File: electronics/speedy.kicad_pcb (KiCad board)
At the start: 2 copper layers, 32 x 32 mm, 131 parts, among them Q1 2N7002, Q2 2N7002, SW1 DFU, SW2 Push, U1 STM32F415RGT6, U10 INA213-SC70, U11 LT1965, U12 MCP73831, U13 DRV8839, U14 DRV8839, U2 NUF2042VX6, U3 MPU-9250, U4 MS5611-01BA, U5 VL53L0X, U6 NRF24L01+, U7 LT1965, U8 LT1965, U9 LTC2955DDB-1, X1 16Mhz 10ppm

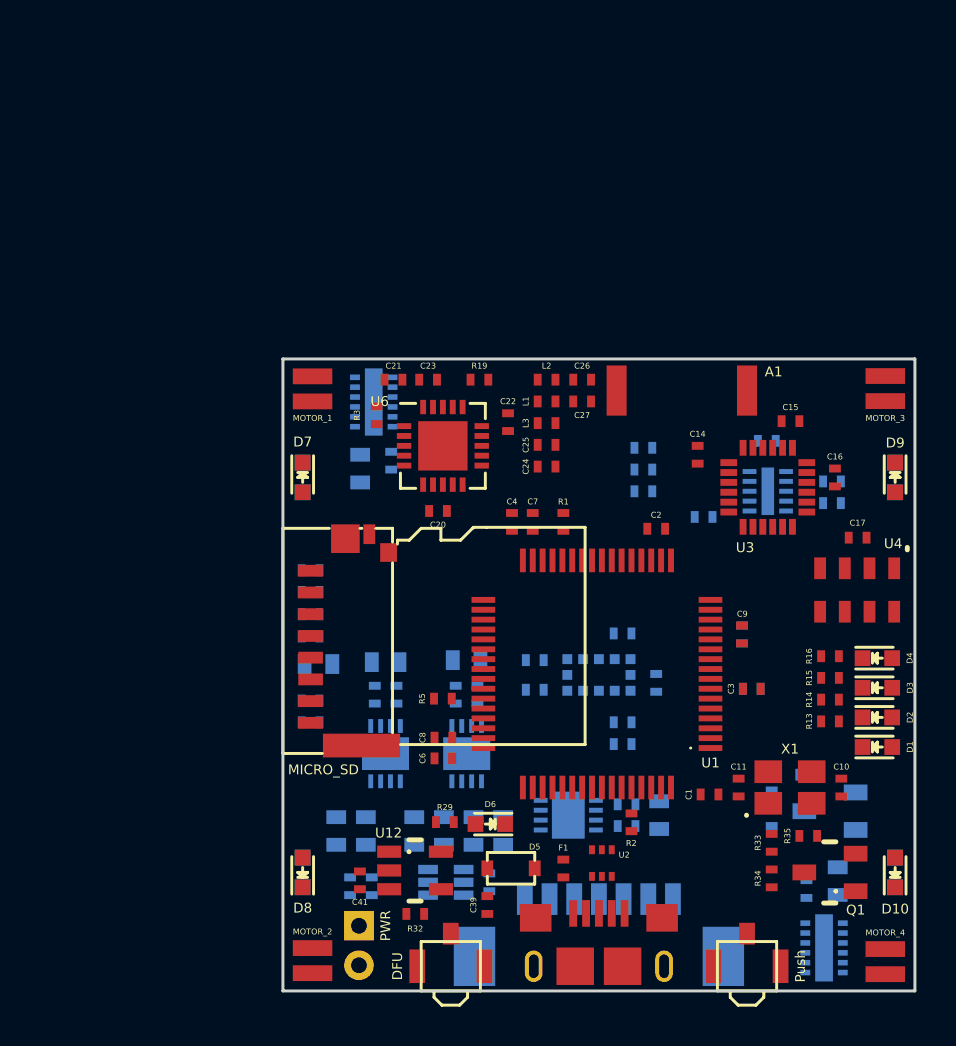
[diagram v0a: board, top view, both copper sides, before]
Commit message: Place components again after schematic update
Increase size of board to 40mmx40mm
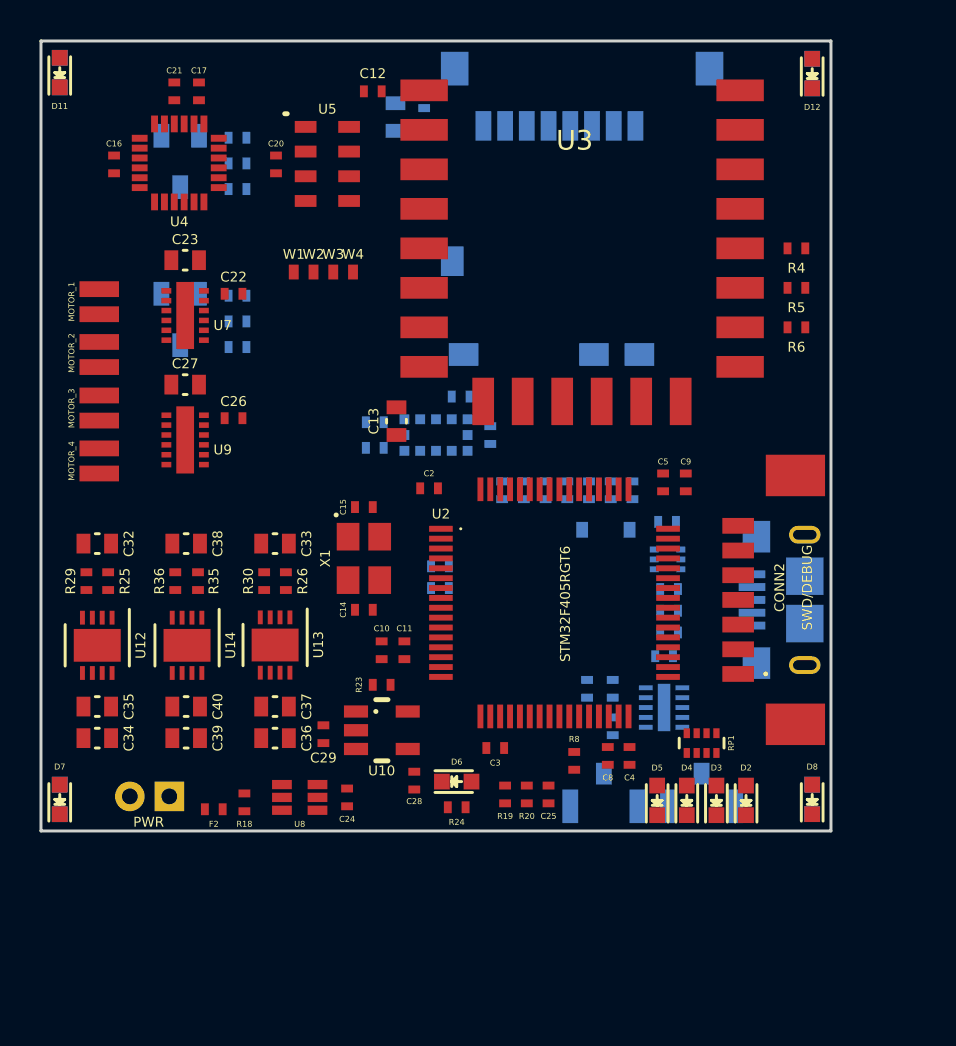
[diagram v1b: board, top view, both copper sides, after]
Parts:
- removed A1: ANTENNA, _div:_ANT-2.45-CHP
- removed C41: 4.7uF, _std:_0402
- removed C42, C45, C46: 10uF, _std:_0603
- removed C43, C44: 0.1uF, _std:_0402
- removed L1: 8.2nH, _std:_0402
- removed L2: 3.9nH, _std:_0402
- removed L3: 2.7nH, _std:_0402
- removed R37: 100, _std:_0402
- removed R38: 40, _std:_0402
- added RP1: 1k, Resistors_SMD:R_Array_Concave_4x0402, F.Cu at (150.8, 110.3)
- added W1: IMU_CS, _div:TestPad, F.Cu at (130.2, 86.5)
- added W2: IMU_SCK, _div:TestPad, F.Cu at (131.2, 86.5)
- added W3: IMU_MISO, _div:TestPad, F.Cu at (132.2, 86.5)
- added W4: IMU_MOSI, _div:TestPad, F.Cu at (133.2, 86.5)
- C1: value 4.7uF -> 0.1uF; moved to B.Cu
- C10: value 10pF -> 1uF
- C11: value 10pF -> 0.1uF
- C12: value 10uF -> 0.1uF; footprint _std:_0603 -> _std:_0402; moved to F.Cu
- C13, C34: value 0.1uF -> 100uF; footprint _std:_0402 -> _std:_0603; moved to F.Cu
- C14: value 0.1uF -> 10pF
- C15: value 10nF -> 10pF
- C17: value 0.1uF -> 10nF
- C2: value 0.1uF -> 4.7uF
- C21: value 33nF -> 0.1uF
- C22: value 10nF -> 0.1uF
- C23: value 1nF -> 10uF; footprint _std:_0402 -> _std:_0603
- C24: value 2.2nF -> 0.1uF
- C25: value 4.7pF -> 0.1uF
- C26: value 1.5pF -> 0.1uF
- C27: value 1pF -> 10uF; footprint _std:_0402 -> _std:_0603
- C28, C29: value 100uF -> 4.7uF; footprint _std:_0603 -> _std:_0402; moved to F.Cu
- C31: value 10uF -> 0.1uF; footprint _std:_0603 -> _std:_0402
- C32, C35, C38, D11, D12, F2, R6: moved to F.Cu
- C33, C40: value 0.1uF -> 10uF; footprint _std:_0402 -> _std:_0603; moved to F.Cu
- C36: value 10uF -> 100uF; moved to F.Cu
- C37: value 100uF -> 10uF; moved to F.Cu
- C39: value 4.7uF -> 100uF; footprint _std:_0402 -> _std:_0603
- C5: value 1uF -> 0.1uF; moved to F.Cu
- C6: value 0.1uF -> 10uF; footprint _std:_0402 -> _std:_0603; moved to B.Cu
- C7: value 2.2uF -> 0.1uF; moved to B.Cu
- C9: value 0.1uF -> 2.2uF
- CONN1: value SWD/DEBUG -> MICRO_USB; footprint _connectors:_Molex-PicoBlade-SMD-7 -> _connectors:_Micro-USB-AB-receptacle-SMT-th
- CONN2: value MICRO_SD -> SWD/DEBUG; footprint _div:_Molex-microSD-WM6701 -> _connectors:_Molex-PicoBlade-SMD-7
- CONN3: value MICRO_USB -> MICRO_SD; footprint _connectors:_Micro-USB-AB-receptacle-SMT-th -> _div:_Molex-microSD-502570-0893; moved to B.Cu
- CONN4: value PWR -> MOTOR_1; footprint _connectors:_Pin2mm_2 -> _connectors:_Solder_Pad1.27_2
- CONN5: value MOTOR_1 -> PWR; footprint _connectors:_Solder_Pad1.27_2 -> _connectors:_Pin2mm_2
- D1: value POWER -> SBR130S3-7; footprint _std:_LED_0603 -> _std:_SOD-323; moved to B.Cu
- D10, D9, Q1, SW1: moved to B.Cu
- D2: value ERROR -> POWER
- D3: value STATUS -> ERROR
- D4: value HEARTBEAT -> STATUS
- D5: value SBR130S3-7 -> DEBUG; footprint _std:_SOD-323 -> _std:_LED_0603
- D6: value CHARGE_LED -> CHARGE
- F1: value 500mA -> 0ZCJ0050AF2E; moved to B.Cu
- R1: value 47k -> 100k; moved to B.Cu
- R13, R16: value 1k -> 10k; moved to B.Cu
- R14, R15: value 1k -> 47k; moved to B.Cu
- R18: value 10k -> 10m; moved to F.Cu
- R19: value 22k -> 2.8k
- R2, R3: value 47k -> 4.7k; moved to B.Cu
- R20: value 10m -> 2k; moved to F.Cu
- R22: value 3.3k -> 10k
- R23: value 2.05k -> 2k; moved to F.Cu
- R24: value 3.3k -> 330; moved to F.Cu
- R25: value 2.05k -> 3.3k; moved to F.Cu
- R26: value 10k -> 3.3k; moved to F.Cu
- R27: value 2.8k -> 100
- R28: value 2k -> 100
- R29: value 330 -> 2.05k
- R30: value 3.3k -> 2.05k; moved to F.Cu
- R31: value 2.05k -> 10k
- R32: value 2k -> 10k; moved to B.Cu
- R33: value 10k -> 40; moved to B.Cu
- R34: value 100 -> 40; moved to B.Cu
- R35: value 40 -> 3.3k
- R36: value 10k -> 2.05k; moved to F.Cu
- R4: value 100k -> 10k; moved to F.Cu
- R5: value 47k -> 10k
- R7: value 4.7k -> 47k
- R8: value 10k -> 47k; moved to F.Cu
- R9: value 4.7k -> 10k
- SW2: value Push -> PushButton; moved to B.Cu
- U1: value STM32F415RGT6 -> NUF2042VX6; footprint _lqfp:_LQFP64 -> _std:SOT-563_6-lead; moved to B.Cu
- U10: value INA213-SC70 -> MCP73831; footprint _std:SC70 -> _std:_TSOT23-5; moved to F.Cu
- U11: value LT1965 -> LTC2955DDB-1; footprint Housings_DFN_QFN:DFN-8-1EP_3x3mm_Pitch0.5mm -> Housings_DFN_QFN:DFN-10-1EP_2x3mm_Pitch0.5mm
- U12: value MCP73831 -> LT1965; footprint _std:_TSOT23-5 -> Housings_DFN_QFN:DFN-8-1EP_3x3mm_Pitch0.5mm
- U13, U14: value DRV8839 -> LT1965; footprint _div:TI-DRV8839_PWSON-N12 -> Housings_DFN_QFN:DFN-8-1EP_3x3mm_Pitch0.5mm; moved to F.Cu
- U2: value NUF2042VX6 -> STM32F405RGT6; footprint _std:SOT-563_6-lead -> _lqfp:_LQFP64
- U3: value MPU-9250 -> ESP-12E; footprint _sensors:_MPU-9XX0 -> _esp:ESP-12-E
- U4: value MS5611-01BA -> MPU-9250; footprint _sensors:_MS5611-01BA -> _sensors:_MPU-9XX0
- U5: value VL53L0X -> MS5611-01BA; footprint _sensors:ST-VL53L0X -> _sensors:_MS5611-01BA; moved to F.Cu
- U6: value NRF24L01+ -> VL53L0X; footprint Housings_DFN_QFN:QFN-20-1EP_4x4mm_Pitch0.5mm -> _sensors:ST-VL53L0X; moved to B.Cu
- U7: value LT1965 -> DRV8839; footprint Housings_DFN_QFN:DFN-8-1EP_3x3mm_Pitch0.5mm -> _div:TI-DRV8839_PWSON-N12; moved to F.Cu
- U8: value LT1965 -> INA213-SC70; footprint Housings_DFN_QFN:DFN-8-1EP_3x3mm_Pitch0.5mm -> _std:SC70; moved to F.Cu
- U9: value LTC2955DDB-1 -> DRV8839; footprint Housings_DFN_QFN:DFN-10-1EP_2x3mm_Pitch0.5mm -> _div:TI-DRV8839_PWSON-N12; moved to F.Cu
- moved Q1 51.9 mm to (123.5, 79.5), turned to 0 degrees
- moved D12 48.0 mm to (156.4, 76.4)
- moved CONN8 47.2 mm to (120.3, 96.0)
- moved D13 47.0 mm to (118.3, 76.3), turned to 90 degrees
- moved D9 45.3 mm to (118.3, 113.2), turned to 90 degrees
- moved R33 44.8 mm to (127.3, 79.7), turned to 0 degrees
- moved Q2 43.3 mm to (123.5, 87.5), turned to 0 degrees
- moved CONN3 42.6 mm to (147.5, 79.0), turned to 180 degrees
- moved D14 40.7 mm to (156.4, 76.4)
- moved U4 40.6 mm to (124.4, 80.9), turned to 180 degrees
- moved C17 40.3 mm to (125.4, 77.3), turned to 90 degrees
- moved R34 40.0 mm to (127.3, 87.7), turned to 0 degrees
- moved CONN7 39.8 mm to (120.3, 93.3), turned to 270 degrees
- moved C16 39.8 mm to (121.1, 81.0), turned to 270 degrees
- moved U14 35.7 mm to (124.8, 105.3)
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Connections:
- C1 pad 1: VCC -> /STM32F4_NRST
- C10 pad 1: Net-(C10-Pad1) -> VCCA
- C11 pad 1: Net-(C11-Pad1) -> VCCA
- C12 pad 1: SD_VCC -> /WIFI_RST_N
- C13 pad 1: SD_VCC -> VCC
- C14 pad 1: VCCA -> Net-(C14-Pad1)
- C15 pad 1: VCCA -> Net-(C15-Pad1)
- C16 pad 1: Net-(C16-Pad1) -> VCCA
- C20 pad 1: VCC -> VCCA
- C21 pad 1: GND -> Net-(C21-Pad1)
- C21 pad 2: Net-(C21-Pad2) -> GND
- C23 pad 1: VCC -> +BATT
- C24 pad 1: Net-(C24-Pad1) -> VCC
- C25 pad 1: Net-(C24-Pad1) -> /VOLTAGE_BAT_SENSE
- C26 pad 1: Net-(C26-Pad1) -> VCC
- C26 pad 2: Net-(A1-Pad1) -> GND
- C27 pad 1: Net-(A1-Pad1) -> +BATT
- C28 pad 1: +BATT -> +5V_protected
- C3 pad 1: /STM32F4_NRST -> VCC
- C31 pad 1: +BATT -> Net-(C31-Pad1)
- C32 pad 1: +BATT -> VCC
- C33 pad 1: Net-(C33-Pad1) -> SD_VCC
- C34 pad 1: VCC -> +BATT
- C35 pad 1: VCC -> +BATT
- C36 pad 1: VCCA -> +BATT
- C38 pad 1: +BATT -> VCCA
- C39 pad 1: /V_USB -> +BATT
- C40 pad 1: /VOLTAGE_BAT_SENSE -> +BATT
- C5 pad 1: VCCA -> VCC
- C6 pad 1: VCC -> SD_VCC
- C7 pad 1: Net-(C7-Pad1) -> SD_VCC
- C9 pad 1: VCCA -> Net-(C9-Pad1)
- CONN1 pad 1: VCC -> Net-(CONN1-Pad1)
- CONN1 pad 2: GND -> Net-(CONN1-Pad2)
- CONN1 pad 3: /STM32F4_NRST -> Net-(CONN1-Pad3)
- CONN1 pad 4: /STM32F4_SWDIO -> Net-(CONN1-Pad4)
- CONN1 pad 5: /STM32F4_SWCLK -> GND
- CONN1 pad 6: /UART3_TX -> Net-(CONN1-Pad6)
- CONN2 pad 1: /SDIO_D2 -> VCC
- CONN2 pad 2: /SDIO_D3 -> GND
- CONN2 pad 3: /SDIO_CMD -> /STM32F4_NRST
- CONN2 pad 4: SD_VCC -> /STM32F4_SWDIO
- CONN2 pad 5: /SDIO_CLK -> /STM32F4_SWCLK
- CONN2 pad 6: GND -> /UART3_TX
- CONN2 pad 7: /SDIO_D0 -> /UART3_RX
- CONN3 pad 1: Net-(CONN3-Pad1) -> /SDIO_D2
- CONN3 pad 2: Net-(CONN3-Pad2) -> /SDIO_D3
- CONN3 pad 3: Net-(CONN3-Pad3) -> /SDIO_CMD
- CONN3 pad 4: Net-(CONN3-Pad4) -> SD_VCC
- CONN3 pad 5: GND -> /SDIO_CLK
- CONN3 pad 6: Net-(CONN3-Pad6) -> GND
- CONN5 pad 1: /Power/MOTOR_1_OUT -> Net-(CONN5-Pad1)
- CONN6 pad 1: /Power/MOTOR_2_OUT -> Net-(CONN6-Pad1)
- CONN7 pad 1: /Power/MOTOR_3_OUT -> Net-(CONN7-Pad1)
- CONN8 pad 1: /Power/MOTOR_4_OUT -> Net-(CONN8-Pad1)
- D1 pad 2: GND -> +5V_protected
- D10 pad 1: Net-(D10-Pad1) -> +BATT
- D11 pad 1: +BATT -> Net-(D11-Pad1)
- D12 pad 1: Net-(D11-Pad2) -> Net-(D12-Pad1)
- D12 pad 2: Net-(D12-Pad2) -> Net-(D11-Pad2)
- D13 pad 1: +BATT -> Net-(D13-Pad1)
- D14 pad 1: Net-(D13-Pad2) -> Net-(D10-Pad2)
- D14 pad 2: Net-(D12-Pad2) -> Net-(D13-Pad2)
- D2 pad 1: Net-(D2-Pad1) -> GND
- D2 pad 2: GND -> Net-(D2-Pad2)
- D3 pad 1: Net-(D3-Pad1) -> GND
- D3 pad 2: GND -> Net-(D3-Pad2)
- D4 pad 1: Net-(D4-Pad1) -> GND
- D4 pad 2: GND -> Net-(D4-Pad2)
- D5 pad 1: Net-(D5-Pad1) -> GND
- D5 pad 2: /V_USB -> Net-(D5-Pad2)
- D6 pad 1: /V_USB -> +5V_protected
- D7 pad 2: Net-(D7-Pad2) -> Net-(D11-Pad1)
- D8 pad 1: Net-(D7-Pad2) -> +BATT
- D8 pad 2: Net-(D10-Pad2) -> Net-(D12-Pad1)
- D9 pad 2: Net-(D10-Pad1) -> Net-(D13-Pad1)
- F1 pad 1: Net-(D5-Pad1) -> Net-(D1-Pad1)
- F1 pad 2: Net-(CONN3-Pad1) -> Net-(CONN1-Pad1)
- F2 pad 1: Net-(CONN4-Pad1) -> Net-(CONN5-Pad1)
- Q1 pad 1: Net-(D10-Pad2) -> Net-(D11-Pad2)
- Q2 pad 1: Net-(D12-Pad2) -> Net-(D13-Pad2)
- R1 pad 1: GND -> VCC
- R1 pad 2: /BOOT1 -> /STM32F4_NRST
- R10 pad 2: /SDIO_D2 -> /SDIO_D1
- R11 pad 2: /SDIO_D3 -> /SDIO_D2
- R12 pad 2: /SDIO_CMD -> /SDIO_D3
- R13 pad 1: Net-(D1-Pad1) -> VCC
- R13 pad 2: VCC -> /SDIO_CMD
- R14 pad 1: Net-(D2-Pad1) -> /WIFI_EN
- R14 pad 2: /ERROR_LED -> GND
- R15 pad 1: Net-(D3-Pad1) -> /MOTOR_2_IN
- R15 pad 2: /STATUS_LED -> GND
- R16 pad 1: Net-(D4-Pad1) -> VCCA
- R16 pad 2: /HEARTBEAT_LED -> /TOF_GPIO1
- R18 pad 1: VCCA -> +BATT
- R18 pad 2: /TOF_GPIO1 -> Net-(F2-Pad2)
- R19 pad 1: Net-(R19-Pad1) -> +BATT
- R19 pad 2: GND -> /VOLTAGE_BAT_SENSE
- R2 pad 1: /BOOT0 -> VCCA
- R2 pad 2: GND -> /I2C1_SCL
- R20 pad 1: +BATT -> /VOLTAGE_BAT_SENSE
- R20 pad 2: Net-(F2-Pad2) -> GND
- R22 pad 1: VCC -> /POWER_KILL
- R22 pad 2: Net-(R22-Pad2) -> VCC
- R23 pad 1: Net-(R22-Pad2) -> Net-(R23-Pad1)
- R24 pad 1: VCCA -> Net-(R24-Pad1)
- R24 pad 2: Net-(R24-Pad2) -> Net-(D6-Pad2)
- R25 pad 1: Net-(R24-Pad2) -> VCC
- R25 pad 2: GND -> Net-(R25-Pad2)
- R26 pad 1: /POWER_KILL -> SD_VCC
- R26 pad 2: VCC -> Net-(R26-Pad2)
- R27 pad 1: +BATT -> Net-(Q1-Pad2)
- R27 pad 2: /VOLTAGE_BAT_SENSE -> /IR_EN_TOP
- R28 pad 1: /VOLTAGE_BAT_SENSE -> Net-(Q2-Pad2)
- R28 pad 2: GND -> /IR_EN_BOTTOM
- R29 pad 1: Net-(R29-Pad1) -> Net-(R25-Pad2)
- R29 pad 2: Net-(D6-Pad2) -> GND
- R3 pad 1: /NRF24L01+_EN -> VCCA
- R3 pad 2: GND -> /I2C1_SDA
- R30 pad 1: SD_VCC -> Net-(R26-Pad2)
- R30 pad 2: Net-(R30-Pad2) -> GND
- R31 pad 1: Net-(R30-Pad2) -> /IR_EN_TOP
- R32 pad 1: Net-(R32-Pad1) -> /IR_EN_BOTTOM
- R33 pad 1: /IR_EN_TOP -> Net-(Q1-Pad3)
- R34 pad 1: Net-(Q1-Pad2) -> Net-(Q2-Pad3)
- R34 pad 2: /IR_EN_TOP -> GND
- R35 pad 1: Net-(Q1-Pad3) -> VCCA
- R35 pad 2: GND -> Net-(R35-Pad2)
- R36 pad 1: /IR_EN_BOTTOM -> Net-(R35-Pad2)
- R4 pad 2: /STM32F4_NRST -> Net-(R4-Pad2)
- R5 pad 1: /MOTOR_2_IN -> VCC
- R5 pad 2: GND -> Net-(R5-Pad2)
- R6 pad 1: VCC -> GND
- R6 pad 2: /SDIO_D0 -> Net-(R6-Pad2)
- R7 pad 1: VCCA -> /BOOT0
- R7 pad 2: /I2C1_SCL -> GND
- R8 pad 1: VCC -> GND
- R8 pad 2: /SDIO_D1 -> /BOOT1
- R9 pad 1: VCCA -> VCC
- R9 pad 2: /I2C1_SDA -> /SDIO_D0
- U1 pad 1: VCC -> /USB_DP
- U1 pad 2: /SD_PWR_EN -> GND
- U1 pad 3: /SD_DETECT -> /USB_DM
- U1 pad 4: /MOTOR_3_EN -> Net-(CONN1-Pad2)
- U1 pad 5: Net-(C11-Pad1) -> +5V_protected
- U1 pad 6: Net-(C10-Pad1) -> Net-(CONN1-Pad3)
- U10 pad 1: GND -> Net-(R24-Pad1)
- U10 pad 3: VCC -> +BATT
- U10 pad 4: +BATT -> +5V_protected
- U10 pad 5: Net-(F2-Pad2) -> Net-(R23-Pad1)
- U11 pad 1: SD_VCC -> /PUSHBUTTON_INT
- U11 pad 2: SD_VCC -> Net-(U11-Pad2)
- U11 pad 3: Net-(R30-Pad2) -> /Power/POWER_EN
- U11 pad 4: GND -> +BATT
- U11 pad 5: GND -> Net-(SW2-Pad1)
- U11 pad 6: /SD_PWR_EN -> GND
- U11 pad 8: +BATT -> Net-(C31-Pad1)
- U11 pad 9: GND -> /POWER_KILL
- U12 pad 1: Net-(R29-Pad1) -> VCC
- U12 pad 2: GND -> VCC
- U12 pad 3: +BATT -> Net-(R25-Pad2)
- U12 pad 4: /V_USB -> GND
- U12 pad 5: Net-(R32-Pad1) -> GND
- U13 pad 1: +BATT -> SD_VCC
- U13 pad 2: +BATT -> SD_VCC
- U13 pad 3: /Power/MOTOR_1_OUT -> Net-(R26-Pad2)
- U13 pad 4: /Power/MOTOR_2_OUT -> GND
- U13 pad 6: GND -> /SD_PWR_EN
- U13 pad 7: /MOTOR_2_EN -> +BATT
- U13 pad 8: /MOTOR_2_IN -> +BATT
- U13 pad 9: /MOTOR_1_EN -> GND
- U14 pad 1: +BATT -> VCCA
- U14 pad 2: +BATT -> VCCA
- U14 pad 3: /Power/MOTOR_3_OUT -> Net-(R35-Pad2)
- U14 pad 4: /Power/MOTOR_4_OUT -> GND
- U14 pad 6: GND -> /SENSOR_PWR_EN
- U14 pad 7: /MOTOR_4_EN -> +BATT
- U14 pad 8: /MOTOR_4_IN -> +BATT
- U14 pad 9: /MOTOR_3_EN -> GND
- U2 pad 1: /USB_DP -> VCC
- U2 pad 2: GND -> /SD_PWR_EN
- U2 pad 3: /USB_DM -> /SD_DETECT
- U2 pad 4: Net-(CONN3-Pad2) -> /MOTOR_3_EN
- U2 pad 5: /V_USB -> Net-(C15-Pad1)
- U2 pad 6: Net-(CONN3-Pad3) -> Net-(C14-Pad1)
- U3 pad 1: Net-(U3-Pad1) -> /WIFI_RST_N
- U3 pad 10: Net-(C16-Pad1) -> /WIFI_MISO
- U3 pad 11: GND -> Net-(U3-Pad11)
- U3 pad 12: /MPU9250_INT -> /WIFI_CS
- U3 pad 13: VCCA -> /WIFI_INT
- U3 pad 14: Net-(U3-Pad14) -> /WIFI_SCK
- U3 pad 15: Net-(U3-Pad15) -> GND
- U3 pad 16: Net-(U3-Pad16) -> Net-(R6-Pad2)
- U3 pad 17: Net-(U3-Pad17) -> Net-(R5-Pad2)
- U3 pad 18: GND -> Net-(R4-Pad2)
- U3 pad 19: VCCA -> Net-(U3-Pad19)
- U3 pad 20: GND -> Net-(U3-Pad20)
- U3 pad 22: /MPU9250_CS -> Net-(U3-Pad22)
- U3 pad 3: Net-(U3-Pad3) -> /WIFI_EN
- U3 pad 8: VCCA -> VCC
- U3 pad 9: /SPI1_MISO -> /WIFI_MOSI
- U4 pad 1: VCCA -> Net-(U4-Pad1)
- U4 pad 2: VCCA -> Net-(U4-Pad2)
- U4 pad 3: GND -> Net-(U4-Pad3)
- U4 pad 4: GND -> Net-(U4-Pad4)
- U4 pad 5: GND -> Net-(U4-Pad5)
- U4 pad 7: /I2C1_SDA -> Net-(U4-Pad7)
- U4 pad 8: /I2C1_SCL -> VCCA
- U5 pad 2: GND -> VCCA
- U5 pad 5: /TOF_XSHUT -> GND
- U5 pad 6: GND -> Net-(U5-Pad6)
- U5 pad 7: /TOF_GPIO1 -> /I2C1_SDA
- U5 pad 8: Net-(U5-Pad8) -> /I2C1_SCL
- U6 pad 1: /NRF24L01+_EN -> VCCA
- U6 pad 10: /MCU_OSC_OUT -> /I2C1_SCL
- U6 pad 11: Net-(C24-Pad1) -> VCCA
- U6 pad 12: Net-(L1-Pad2) -> GND
- U6 pad 2: /NRF24L01+_CS -> GND
- U6 pad 3: /SPI2_SCK -> GND
- U6 pad 4: /SPI2_MOSI -> GND
- U6 pad 5: /SPI2_MISO -> /TOF_XSHUT
- U6 pad 6: /NRF24L01+_INT -> GND
- U6 pad 7: VCC -> /TOF_GPIO1
- U6 pad 8: GND -> Net-(U6-Pad8)
- U6 pad 9: Net-(U6-Pad9) -> /I2C1_SDA
- U7 pad 1: VCC -> +BATT
- U7 pad 2: VCC -> +BATT
- U7 pad 3: Net-(R22-Pad2) -> Net-(CONN4-Pad1)
- U7 pad 4: GND -> Net-(CONN6-Pad1)
- U7 pad 6: /Power/POWER_EN -> GND
- U7 pad 7: +BATT -> /MOTOR_2_EN
- U7 pad 8: +BATT -> /MOTOR_2_IN
- U7 pad 9: GND -> /MOTOR_1_EN
- U8 pad 1: VCCA -> GND
- U8 pad 2: VCCA -> GND
- U8 pad 3: Net-(R24-Pad2) -> VCC
- U8 pad 4: GND -> +BATT
- U8 pad 5: GND -> Net-(F2-Pad2)
- U8 pad 6: /SENSOR_PWR_ON -> /CURRENT_BAT_SENSE
- U9 pad 1: /PUSHBUTTON_INT -> +BATT
- U9 pad 10: GND -> /MOTOR_3_IN
- U9 pad 11: (no net) -> VCC
- U9 pad 2: Net-(U9-Pad2) -> +BATT
- U9 pad 3: /Power/POWER_EN -> Net-(CONN7-Pad1)
- U9 pad 4: +BATT -> Net-(CONN8-Pad1)
- U9 pad 5: Net-(SW2-Pad1) -> GND
- U9 pad 7: +BATT -> /MOTOR_4_EN
- U9 pad 8: Net-(C33-Pad1) -> /MOTOR_4_IN
- U9 pad 9: /POWER_KILL -> /MOTOR_3_EN
- X1 pad 1: Net-(C11-Pad1) -> Net-(C15-Pad1)
- X1 pad 3: Net-(C10-Pad1) -> Net-(C14-Pad1)
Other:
- board size 32 x 32 mm -> 40 x 40 mm

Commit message: Update with small corrections
Decrease LED resistor values
Fix NUF2042 name
Fix MPU9250 wiring (contradictory datasheet)
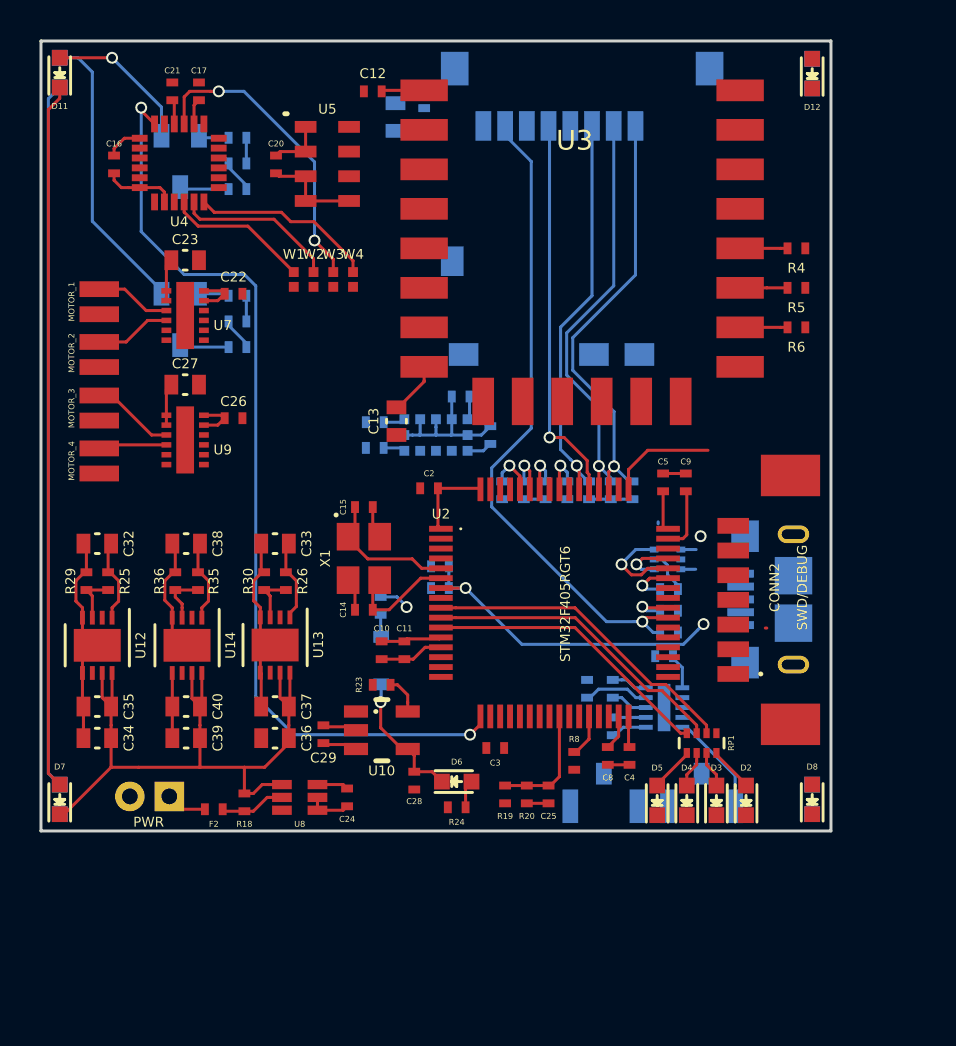
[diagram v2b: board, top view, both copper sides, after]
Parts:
- RP1: value 1k -> 330
- U1: value NUF2042VX6 -> NUF2042XV6
- moved F1 15.1 mm to (134.6, 103.3), turned to 90 degrees
- moved D1 13.2 mm to (134.6, 106.1), turned to 270 degrees
- moved CONN1 0.58 mm to (155.5, 103.0)
- moved CONN2 0.25 mm to (155.3, 102.4)
- moved C21 0.10 mm to (124.0, 77.3)
- turned R7 to 270 degrees
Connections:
- U4 pad 1: Net-(U4-Pad1) -> VCCA
- U4 pad 19: VCCA -> Net-(U4-Pad19)
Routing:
- net GND: track 0.00 -> 65.9 mm
- net /IMU_INT: track 0.00 -> 47.9 mm, vias 0 -> 2
- net +BATT: track 0.00 -> 43.6 mm
- net Net-(D11-Pad1): track 0.00 -> 35.8 mm
- net Net-(D13-Pad1): track 0.00 -> 35.8 mm
- net /SDIO_D0: track 0.00 -> 33.2 mm, vias 0 -> 1
- net VCC: track 0.00 -> 23.3 mm
- net /SDIO_D2: track 0.00 -> 21.9 mm, vias 0 -> 1
- net /SDIO_D3: track 0.00 -> 21.1 mm, vias 0 -> 1
- net /SDIO_CMD: track 0.00 -> 20.5 mm, vias 0 -> 1
- net /SDIO_CLK: track 0.00 -> 19.7 mm, vias 0 -> 1
- net Net-(CONN1-Pad1): track 0.00 -> 18.6 mm, vias 0 -> 2
- net VCCA: track 0.00 -> 17.1 mm
- net /STM32F4_NRST: track 0.00 -> 16.9 mm, vias 0 -> 2
- net /ERROR_LED: track 0.00 -> 16.3 mm
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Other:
- copper layers 2 -> 4
- net class Default: clearance 0.2 -> 0.154; trace_width 0.25 -> 0.154
- rule trace_clearance: 0.2 -> 0.154
- rule trace_min: 0.2 -> 0.154
- board text added: "Speedy nanocopter v1.0 Salah-Eddine Missri @syrianspock"

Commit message: Finish routing
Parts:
- C13, C23, C27, C32, C33, C34, C35, C36, C37, C38, C39, C40, C6: footprint _std:_0603 -> _std:C_0603
- D10, D11, D12, D13, D14, D2, D3, D4, D5, D6, D7, D8, D9: footprint _std:_LED_0603 -> _std:D_0603
- moved R8 1.71 mm to (144.2, 112.9)
- moved C10 0.55 mm to (135.1, 106.0)
- moved C11 0.55 mm to (136.2, 106.0)
- moved C16 0.45 mm to (121.5, 81.0)
- moved C17 0.36 mm to (125.3, 77.7)
- moved C21 0.36 mm to (124.0, 77.7)
- moved CONN7 0.20 mm to (120.3, 93.5)
- moved CONN8 0.20 mm to (120.3, 96.2)
- moved X1 0.16 mm to (133.7, 100.8)
- moved C14 0.16 mm to (133.7, 103.4)
- moved C15 0.16 mm to (133.7, 98.2)
- moved CONN2 0.06 mm to (155.3, 102.5)
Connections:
- U2 pad 10: /STATUS_LED -> /MOTOR_1_EN
- U2 pad 11: /DEBUG_LED -> /MOTOR_2_EN
- U2 pad 14: /TOF_XSHUT -> /ERROR_LED
- U2 pad 15: /POWER_KILL -> /STATUS_LED
- U2 pad 16: /PUSHBUTTON_INT -> /DEBUG_LED
- U2 pad 26: /MOTOR_1_EN -> /POWER_KILL
- U2 pad 27: /MOTOR_2_EN -> /PUSHBUTTON_INT
- U2 pad 41: /WIFI_RST_N -> /IR_EN_BOTTOM
- U2 pad 50: /TOF_GPIO1 -> /WIFI_RST_N
- U2 pad 57: /MOTOR_4_EN -> /TOF_XSHUT
- U2 pad 62: /IR_EN_BOTTOM -> /TOF_GPIO1
- U2 pad 9: /ERROR_LED -> /MOTOR_4_EN
- U7 pad THRM: (no net) -> GND
- U9 pad THRM: (no net) -> GND
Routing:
- net GND: track 65.9 -> 234.3 mm, vias 0 -> 42
- net +BATT: track 43.6 -> 138.6 mm, vias 0 -> 4
- net VCCA: track 17.1 -> 95.3 mm, vias 0 -> 8
- net /IR_EN_BOTTOM: track 1.67 -> 50.7 mm, vias 0 -> 2
- net /BOOT0: track 2.37 -> 43.0 mm
- net /SDIO_D1: track 2.31 -> 40.2 mm, vias 1 -> 3
- net Net-(D13-Pad2): track 14.6 -> 51.9 mm
- net SD_VCC: track 4.21 -> 41.1 mm, vias 0 -> 2
- net Net-(D10-Pad2): track 0.00 -> 35.8 mm
- net Net-(D12-Pad1): track 0.00 -> 35.8 mm
- net Net-(D11-Pad2): track 7.64 -> 43.1 mm
- net /Power/POWER_EN: track 0.00 -> 33.8 mm, vias 0 -> 2
- net /MOTOR_2_IN: track 2.43 -> 36.1 mm, vias 1 -> 3
- net /MOTOR_1_IN: track 0.00 -> 32.9 mm, vias 0 -> 2
- net /WIFI_RST_N: track 2.17 -> 33.8 mm, vias 0 -> 2
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- added copper zone on In1.Cu, net GND
- added copper zone on In2.Cu, net VCC
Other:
- net class Default: clearance 0.154 -> 0.16; trace_width 0.154 -> 0.16
- rule trace_clearance: 0.154 -> 0.16
